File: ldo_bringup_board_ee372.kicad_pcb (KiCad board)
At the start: 4 copper layers, 100 x 100 mm, 152 parts, among them J1 VIN, J10 MD_SW_EN, J11 MD_MCU_PU_EN, J12 BUF_EN, J13 VSIG, J14 VSIG_BUF, J15 NR, J16 NOISE_X100, J17 NOISE_X1000, J18 VIN_PROBE, J19 VREF_PROBE, J2 GND, J20 VOUT_PROBE, J21 VG0_PROBE, J22 VG1_PROBE, J23 VG2_PROBE, J24 VG3_PROBE, J25 VG4_PROBE, J3 IBIAS, J4 VOUT, J5 VIN_SMA, J6 VOUT_SMA, J7 GND, J8 5V, J9 MD_MCU_EN, Q1 FDV305N, Q2 FDV305N, Q3 FDV305N, Q4 FDV305N, Q5 FDV305N, Q6 FDV305N, SW1 MD_SW, U1 LDO_DualMode_BGR_EE372, U2 Teensy4.1, U3 INA190A5IDDFR, U4 INA190A5IDDFR, U5 OPA4388IDR, U6 BUF602ID, U7 ADT7310TRZ

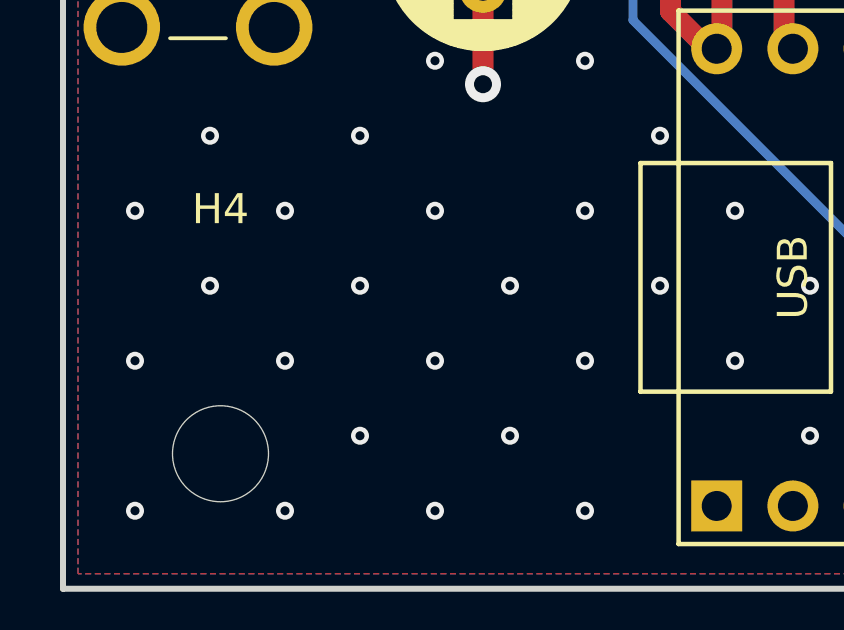
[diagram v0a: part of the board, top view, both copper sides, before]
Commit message: Checkpoint: add group number and date to the silkscreen
One new F.SilkS text, "Grp 3" and "10/4/2026". Nothing else changed.
DRC 0 errors, 0 unconnected, schematic parity 0.
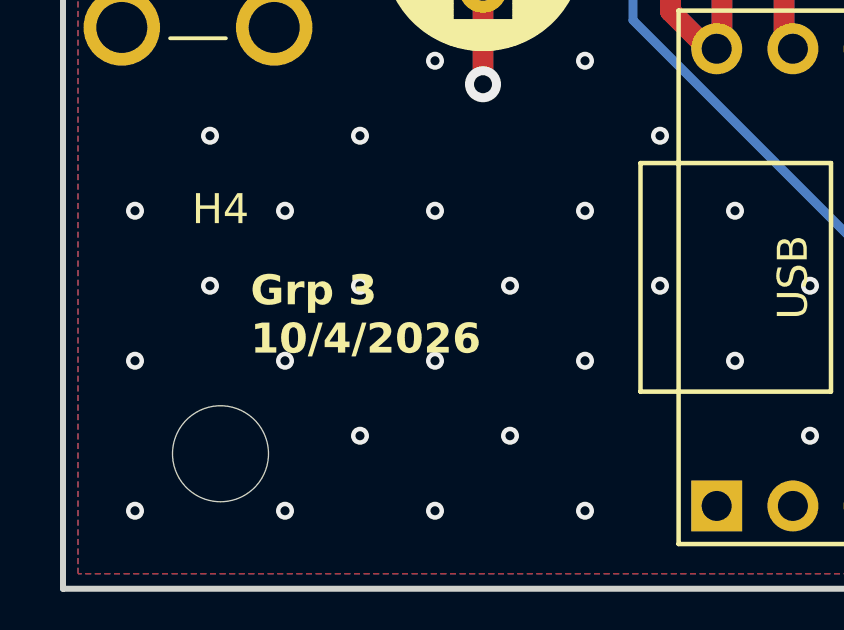
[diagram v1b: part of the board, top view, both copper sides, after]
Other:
- board text added: "Grp 3 10/4/2026"
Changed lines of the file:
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@@
+		)
+	)
+	(gr_text "Grp 3\n10/4/2026"
+		(at 106.25 142.75 0)
+		(layer "F.SilkS")
+		(effects
+			(font
+				(size 1 1)
+				(thickness 0.1875)
+				(bold yes)
+			)
+			(justify left bottom)
 		)
 	)
